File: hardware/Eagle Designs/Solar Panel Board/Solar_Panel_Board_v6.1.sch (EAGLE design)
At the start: 37 parts, among them J1 MOLEX_503763-0291MOLEX_503763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, J2 MOLEX_503763-0491MOLEX_503763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, J3 MOLEX_503763-0291MOLEX_503763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, U1 TMP36GSZ

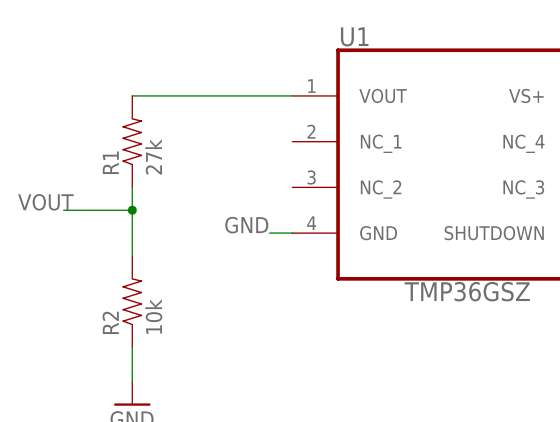
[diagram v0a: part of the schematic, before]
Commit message: Updated solar panel board temp sensor circuit
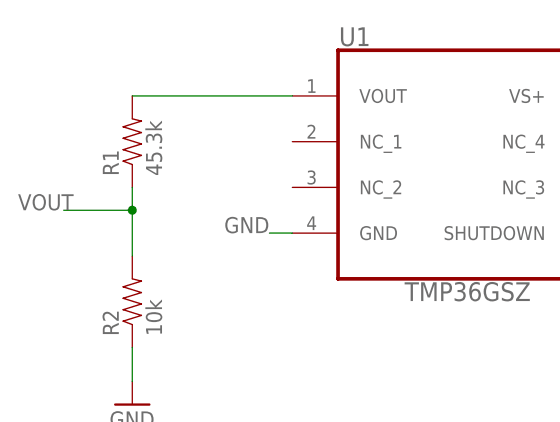
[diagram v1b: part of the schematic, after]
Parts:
- R1: value 27k -> 45.3k
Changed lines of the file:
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@@
 <part name="P+2" library="supply1" library_urn="urn:adsk.eagle:library:371" deviceset="VCC" device=""/>
 <part name="P+7" library="supply1" library_urn="urn:adsk.eagle:library:371" deviceset="VCC" device=""/>
-<part name="R1" library="HSFL_Main_Library" deviceset="RESISTOR" device="0805-RES" value="27k"/>
+<part name="R1" library="HSFL_Main_Library" deviceset="RESISTOR" device="0805-RES" value="45.3k"/>
 <part name="R2" library="HSFL_Main_Library" deviceset="RESISTOR" device="0805-RES" value="10k"/>
 <part name="GND12" library="supply1" library_urn="urn:adsk.eagle:library:371" deviceset="GND" device=""/>
